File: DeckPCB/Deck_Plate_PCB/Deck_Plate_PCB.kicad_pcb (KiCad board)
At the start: 2 copper layers, 101.6 x 53.3 mm, 29 parts, among them J1 Raspberry_Pi_2_3, J2 DB37_Male_MountingHoles, J3 NASA PWR_Interface, P1 Digital, P10 CONN_01X01, P11 CONN_01X01, P12 CONN_01X01, P13 CONN_01X01, P2 Power, P3 Analog, P4 Analog, P5 PWM, P6 PWM, P7 Communication, P8 CONN_01X01, P9 CONN_01X01, Q2 2N7000, Q3 2N7000, U1 Adafruit_INA219_Breakout, U2 LM2576T-5, U3 D24V25F9, U4 SunnyBuddy_Breakout, U5 LM2576T-5, U6 SF_Logic_Level_Conv, U7 LIDAR-LITE_V4_Range, U8 ADXL377

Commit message: Updated RaspPi connections based on input from Software. Updated footprints from capacitor and inductor changes. Added inhibit header for batter, motor, and burn-wire.
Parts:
- added C1: 1000uF, Deck_Plate_PCB:1000uF_Cap, F.Cu at (307.2, 140.2)
- added C2: 1000uF, Deck_Plate_PCB:1000uF_Cap, F.Cu at (293.2, 140.2)
- added C3: 1uF, Capacitor_SMD:C_1206_3216Metric_Pad1.42x1.75mm_HandSolder, F.Cu at (283.4, 124.0)
- added C4: 1uF, Capacitor_SMD:C_1206_3216Metric_Pad1.42x1.75mm_HandSolder, F.Cu at (283.7, 126.7)
- added C5: 220uF, Deck_Plate_PCB:220uF_Cap, F.Cu at (326.8, 135.8)
- added D1: LED, LED_THT:LED_D3.0mm_Clear, F.Cu at (289.7, 125.3)
- added H1: Sunny, MountingHole:MountingHole_2.5mm, F.Cu at (229.7, 106.7)
- added H10: ADXL377, MountingHole:MountingHole_2.5mm, F.Cu at (216.1, 99.2)
- added H11: ADXL377, MountingHole:MountingHole_2.5mm, F.Cu at (216.3, 106.7)
- added H12: ADXL377, MountingHole:MountingHole_2.5mm, F.Cu at (241.8, 99.2)
- added H2: Sunny, MountingHole:MountingHole_2.5mm, F.Cu at (222.8, 113.3)
- added H3: Sunny, MountingHole:MountingHole_2.5mm, F.Cu at (229.2, 99.2)
- added H4: Sunny, MountingHole:MountingHole_2.5mm, F.Cu at (235.3, 105.7)
- added H5: INA219, MountingHole:MountingHole_2.5mm, F.Cu at (222.6, 99.2)
- added H6: INA219, MountingHole:MountingHole_2.5mm, F.Cu at (229.4, 113.3)
- added H7: INA219, MountingHole:MountingHole_2.5mm, F.Cu at (235.3, 99.2)
- added H8: INA219, MountingHole:MountingHole_2.5mm, F.Cu at (216.3, 113.3)
- added H9: ADXL377, MountingHole:MountingHole_2.5mm, F.Cu at (222.8, 106.7)
- added J4: Inhibit_Header, Connector_PinHeader_2.54mm:PinHeader_1x06_P2.54mm_Vertical, F.Cu at (66.9, 218.0)
- added L1: 100uH, Inductor_THT:L_Axial_L5.3mm_D2.2mm_P2.54mm_Vertical_Vishay_IM-1, F.Cu at (282.4, 133.0)
- added L2: 100uH, Inductor_THT:L_Axial_L5.3mm_D2.2mm_P2.54mm_Vertical_Vishay_IM-1, F.Cu at (288.5, 132.9)
- added R1: 220, Resistor_THT:R_Axial_DIN0207_L6.3mm_D2.5mm_P10.16mm_Horizontal, F.Cu at (252.1, 132.1)
- added R10: 10K, Resistor_THT:R_Axial_DIN0207_L6.3mm_D2.5mm_P10.16mm_Horizontal, F.Cu at (252.0, 124.4)
- added R11: 5K, Resistor_THT:R_Axial_DIN0207_L6.3mm_D2.5mm_P10.16mm_Horizontal, F.Cu at (252.0, 128.4)
- added R12: 5K, Resistor_THT:R_Axial_DIN0207_L6.3mm_D2.5mm_P10.16mm_Horizontal, F.Cu at (265.4, 124.4)
- added R13: 10K, Resistor_THT:R_Axial_DIN0207_L6.3mm_D2.5mm_P10.16mm_Horizontal, F.Cu at (252.0, 135.8)
- added R2: 1K, Resistor_THT:R_Axial_DIN0207_L6.3mm_D2.5mm_P10.16mm_Horizontal, F.Cu at (238.0, 140.5)
- added R3: R, Resistor_THT:R_Axial_DIN0207_L6.3mm_D2.5mm_P10.16mm_Horizontal, F.Cu at (238.0, 136.5)
- added R4: 1K, Resistor_THT:R_Axial_DIN0207_L6.3mm_D2.5mm_P10.16mm_Horizontal, F.Cu at (265.3, 136.4)
- added R5: R, Resistor_THT:R_Axial_DIN0207_L6.3mm_D2.5mm_P10.16mm_Horizontal, F.Cu at (238.0, 132.4)
- added R6: 10K, Resistor_THT:R_Axial_DIN0207_L6.3mm_D2.5mm_P10.16mm_Horizontal, F.Cu at (238.0, 128.4)
- added R7: 10K, Resistor_THT:R_Axial_DIN0207_L6.3mm_D2.5mm_P10.16mm_Horizontal, F.Cu at (265.4, 128.4)
- added R8: 5K, Resistor_THT:R_Axial_DIN0207_L6.3mm_D2.5mm_P10.16mm_Horizontal, F.Cu at (265.3, 132.4)
- added R9: 5K, Resistor_THT:R_Axial_DIN0207_L6.3mm_D2.5mm_P10.16mm_Horizontal, F.Cu at (238.0, 124.3)
- added U10: LM20, Deck_Plate_PCB:LM20, F.Cu at (86.1, 206.0)
- added U11: Big_Easy_Driver, Deck_Plate_PCB:Big_Easy_Driver, F.Cu at (56.6, 237.8)
- added U13: LM20, Deck_Plate_PCB:LM20, F.Cu at (81.2, 205.9)
- added U14: Sunny_Batt, Connector_JST:JST_PH_B2B-PH-K_1x02_P2.00mm_Vertical, F.Cu at (75.2, 203.1)
- added U9: TTL_Camera, Connector_PinHeader_2.54mm:PinHeader_1x04_P2.54mm_Vertical, F.Cu at (66.5, 202.6)
- J2: value DB37_Male_MountingHoles -> NASA_Telemetry_Interface
- moved Q2 38.2 mm to (228.0, 125.4)
- moved Q3 38.2 mm to (228.0, 131.2)
- moved U2 27.1 mm to (214.1, 125.8)
- moved D2 26.8 mm to (190.7, 125.0)
- moved D3 24.4 mm to (190.9, 134.2)
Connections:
- net /Bit_16 renamed Net-(J1-Pad22)
- J1 pad 15: /Bit_13 -> Net-(J1-Pad15)
- J1 pad 16: /Bit_14 -> Net-(J1-Pad16)
- J1 pad 18: /Bit_15 -> Net-(J1-Pad18)
- J1 pad 21: /Bit_10 -> Net-(J1-Pad21)
- J1 pad 24: /Bit_9 -> /Strobe
- J1 pad 26: /Bit_8 -> /Bit_7
- J1 pad 27: /Bit_1 -> /Bit_0
- J1 pad 28: /Bit_2 -> /Bit_1
- J1 pad 29: /Bit_6 -> /Bit_5
- J1 pad 3: /Bit_3 -> /Bit_2
- J1 pad 31: /Bit_7 -> /Bit_6
- J1 pad 37: /Strobe -> Net-(J1-Pad37)
- J1 pad 38: /Bit_11 -> Net-(J1-Pad38)
- J1 pad 40: /Bit_12 -> Net-(J1-Pad40)
- J1 pad 5: /Bit_4 -> /Bit_3
- J1 pad 7: /Bit_5 -> /Bit_4
- J2 pad 0: Net-(J2-Pad0) -> GND
- J3 pad 0: Net-(J3-Pad0) -> GND
- U6 pad 1: /2(**) -> Net-(U6-Pad1)
- U6 pad 2: /3(**) -> Net-(U6-Pad2)
- U6 pad 7: /GPIO_A -> Net-(U6-Pad7)
- U6 pad 8: /GPIO_B -> Net-(U6-Pad8)
- U6 pad 9: /??? -> /3v3_Range
- U7 pad 1: /5V_Bus_2 -> /3v3_Range

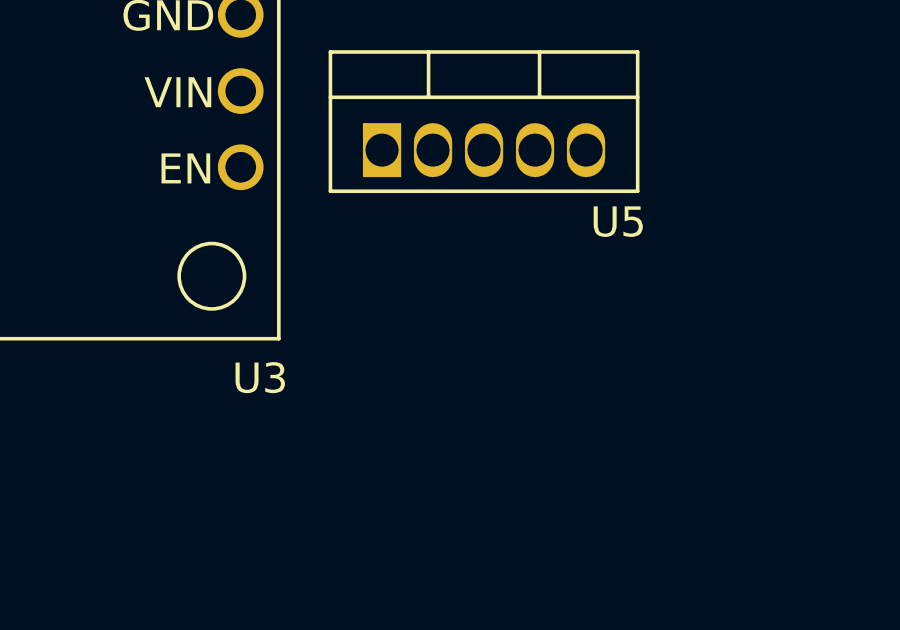
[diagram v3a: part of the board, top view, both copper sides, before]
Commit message: Assigned signals between arduino and sensors based on software input.
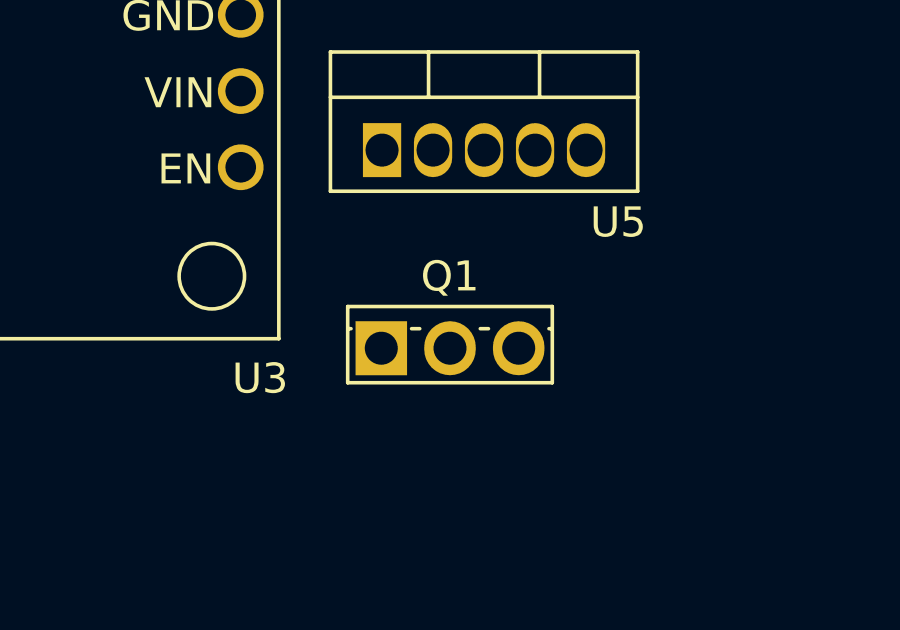
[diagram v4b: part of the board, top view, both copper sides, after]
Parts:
- added Q1: Q_NPN_BCE, Package_TO_SOT_THT:TO-251-3_Vertical, F.Cu at (164.1, 140.7)
- R3, R5: value R -> 4.7
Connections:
- net /24 renamed /Digital_24
- net /25 renamed /Digital_25
- net /26 renamed /Digital_26
- net /27 renamed /Digital_27
- net /28 renamed /Digital_28
- net /29 renamed /Digital_29
- net /30 renamed /Digital_30
- net /31 renamed /Digital_31
- net /32 renamed /Digital_32
- net /33 renamed /Digital_33
- net /34 renamed /Digital_34
- net /35 renamed /Digital_35
- net /36 renamed /Digital_36
- net /37 renamed /Digital_37
- net /38 renamed /Digital_38
- net /39 renamed /Digital_39
- net /40 renamed /Digital_40
- net /41 renamed /Digital_41
- net /42 renamed /Digital_42
- net /44 renamed /Digital_44
- net /45 renamed /Digital_45
- net /46 renamed /Digital_46
- net /47 renamed /Digital_47
- net /48 renamed /Digital_48
- net /49 renamed /Digital_49
- net /TE_Ra renamed /TE_RA
- net /TE_Rb renamed /TE_RB
- P1 pad 14: /43 -> /BurnWireSignal
- P1 pad 33: /22 -> /TE_B
- P1 pad 34: /23 -> /TE_A
- P4 pad 1: /A8 -> /Xout
- P4 pad 2: /A9 -> /Yout
- P4 pad 3: /A10 -> /Zout
- P4 pad 7: /A14 -> /PayloadTemp
- P4 pad 8: /A15 -> /SolarArrayTemp
- P7 pad 5: /18(Tx1) -> /TTL_TX
- P7 pad 6: /19(Rx1) -> /TTL_RX
- R3 pad 1: Net-(Q1-Pad1) -> Net-(Q1-Pad3)
- R3 pad 2: /BurnWireSignal -> GND
- R5 pad 1: /5V_Bus_1 -> Net-(Q1-Pad3)
- R5 pad 2: Net-(Q1-Pad2) -> GND
- U1 pad 3: /SCL -> /21(SCL)
- U1 pad 4: /SDA -> /20(SDA)
- U2 pad 1: /NASA_28V -> /28V_GSE_2
- U5 pad 1: /NASA_28V -> /28V_GSE_2
- U8 pad 5: /A0 -> /Zout
- U8 pad 6: /A1 -> /Yout
- U8 pad 7: /A2 -> /Xout

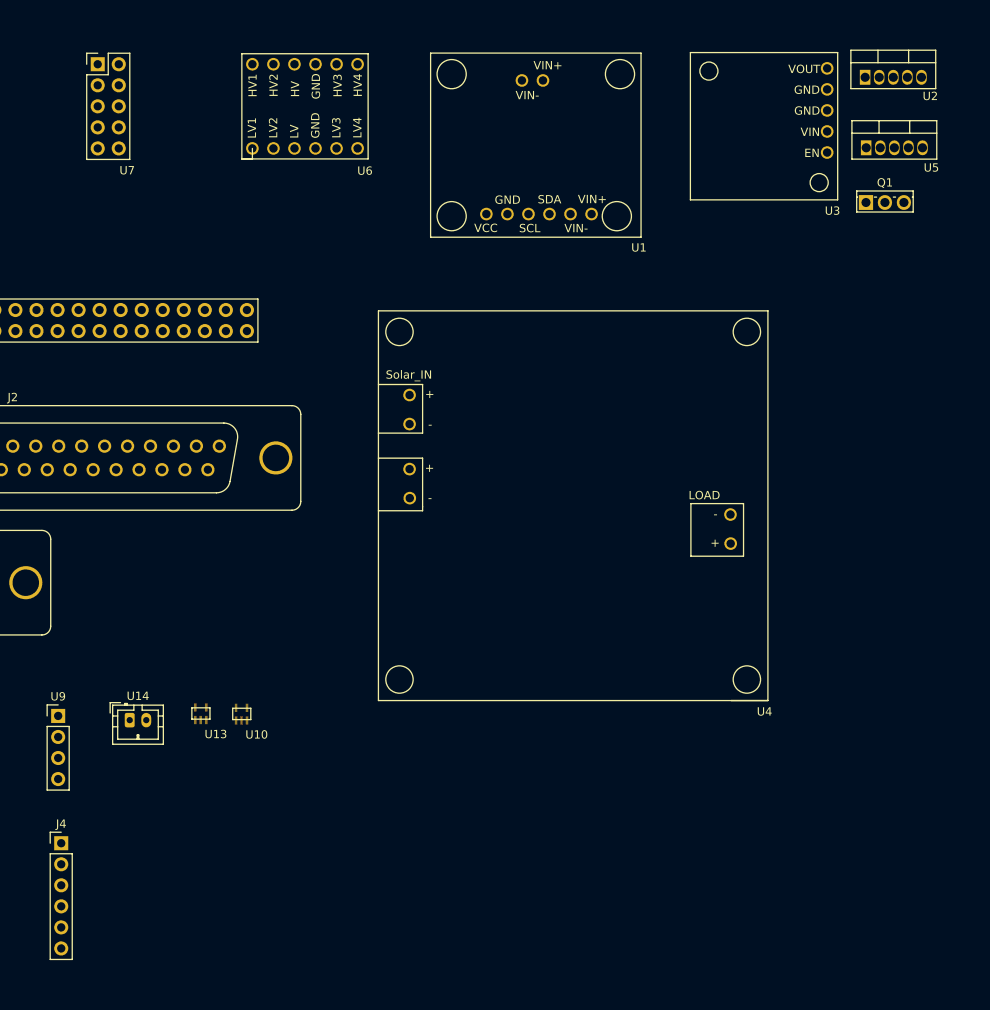
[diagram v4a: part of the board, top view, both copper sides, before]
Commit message: Updated connections to Logic Level Shifter and LiDAR sensor. Updated inhibit connection scheme.
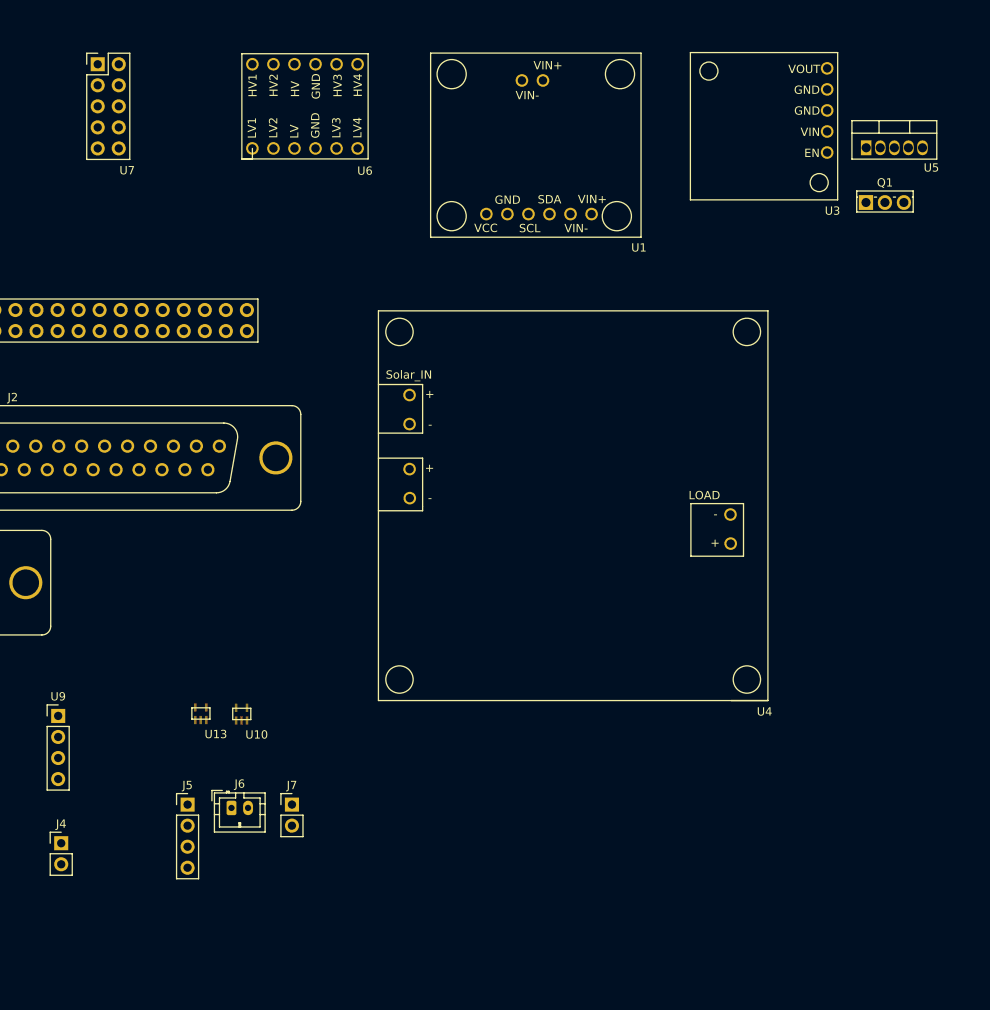
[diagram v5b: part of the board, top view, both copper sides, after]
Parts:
- removed U14: Sunny_Batt, Connector_JST:JST_PH_B2B-PH-K_1x02_P2.00mm_Vertical
- removed the U2 at (164.0, 125.6)
- added J5: SunnyBuddy_Inhibit, Connector_PinHeader_2.54mm:PinHeader_1x04_P2.54mm_Vertical, F.Cu at (82.2, 213.3)
- added J6: Batt_JST_Conn, Connector_JST:JST_PH_B2B-PH-K_1x02_P2.00mm_Vertical, F.Cu at (87.5, 213.7)
- added J7: BurWire_Inhibit, Connector_PinHeader_2.54mm:PinHeader_1x02_P2.54mm_Vertical, F.Cu at (94.8, 213.3)
- J4: value Inhibit_Header -> Motor_Inhibit; footprint Connector_PinHeader_2.54mm:PinHeader_1x06_P2.54mm_Vertical -> Connector_PinHeader_2.54mm:PinHeader_1x02_P2.54mm_Vertical
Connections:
- net /Analog_10 renamed Net-(J2-Pad10)
- net /Analog_4 renamed /NASA_Analog_4
- net /Analog_5 renamed Net-(J2-Pad5)
- net /Analog_6 renamed Net-(J2-Pad6)
- net /Analog_7 renamed Net-(J2-Pad7)
- net /Analog_8 renamed Net-(J2-Pad8)
- net /Analog_9 renamed Net-(J2-Pad9)
- net /Bit_10 renamed Net-(J2-Pad23)
- net /Bit_11 renamed Net-(J2-Pad24)
- net /Bit_12 renamed Net-(J2-Pad25)
- net /Bit_13 renamed Net-(J2-Pad26)
- net /Bit_14 renamed Net-(J2-Pad27)
- net /Bit_15 renamed Net-(J2-Pad28)
- net /Bit_16_LSB renamed Net-(J2-Pad29)
- net /Bit_1_MSB renamed Net-(J2-Pad11)
- net /Bit_8 renamed Net-(J2-Pad21)
- net /Bit_9 renamed Net-(J2-Pad22)
- net /GPIO_A renamed Net-(U7-Pad5)
- net /GPIO_B renamed Net-(U7-Pad6)
- net /LED+ renamed Net-(R1-Pad1)
- J2 pad 1: /Analog_1 -> /NASA_Analog_1
- J2 pad 2: /Analog_2 -> /NASA_Analog_2
- J2 pad 3: /Analog_3 -> /NASA_Analog_3
- J4 pad 1: /Sunny_Batt -> /9V_Bus
- J4 pad 2: GND -> /9V_Bus
- P6 pad 4: /4(**) -> /NASA_Analog_3
- P6 pad 5: /3(**) -> /NASA_Analog_2
- P6 pad 6: /2(**) -> /NASA_Analog_1
- U6 pad 9: /3v3_Range -> +3V3
- U7 pad 1: /3v3_Range -> /5V_Bus_1

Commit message: Initial PCB component placement finished. All mounting holes in place. NOT REPRESENTED: SunnyBuddy, INA219, Electrical inhibits, Motor circuitry, sensor end-panel circuitry. Will create daughter board for these components along with placement for the RaspPi next.
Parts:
- removed H11, H12: ADXL377, MountingHole:MountingHole_2.5mm
- removed H5, H6, H7, H8: INA219, MountingHole:MountingHole_2.5mm
- added H13: Enclos, MountingHole:MountingHole_3.5mm, F.Cu at (45.7, 20.4)
- added H14: Enclos, MountingHole:MountingHole_3.5mm, F.Cu at (45.8, 110.5)
- added H15: Enclos, MountingHole:MountingHole_3.5mm, F.Cu at (155.8, 20.4)
- added H16: Enclos, MountingHole:MountingHole_3.5mm, F.Cu at (155.8, 110.5)
- H1, H2: value Sunny -> 9V_mount; footprint MountingHole:MountingHole_2.5mm -> MountingHole:MountingHole_2.2mm_M2
- H10, H9: value ADXL377 -> Accel_mount
- H3, H4: value Sunny -> Accel_mount
- J2: footprint Connector_Dsub:DSUB-37_Male_Vertical_P2.77x2.84mm_MountingHoles -> Deck_Plate_PCB:NASA_Telem_37-pin_DSub
- J3: footprint Connector_Dsub:DSUB-15_Male_Vertical_P2.77x2.84mm_MountingHoles -> Deck_Plate_PCB:NASA_PWR_15-pin_DSub
- U7: value LIDAR-LITE_V4_Range -> Lidar_RangeFinder; footprint Connector_PinHeader_2.54mm:PinHeader_2x05_P2.54mm_Vertical -> Connector_PinHeader_2.54mm:PinHeader_1x04_P2.54mm_Vertical
- moved C4 326.9 mm to (-41.4, 160.8)
- moved C3 326.2 mm to (-41.7, 149.9)
- moved R4 322.7 mm to (-56.5, 160.7)
- moved D1 319.6 mm to (-20.4, 48.4)
- moved R3 286.6 mm to (-48.5, 129.3)
- moved R2 284.4 mm to (-46.3, 149.8), turned to 180 degrees
- moved R5 277.5 mm to (-39.4, 123.7)
- moved R1 271.8 mm to (-10.5, 61.9), turned to 180 degrees
- moved U4 222.9 mm to (-48.8, -7.44)
- moved R7 216.7 mm to (51.9, 90.6), turned to 180 degrees
- moved Q1 215.9 mm to (-51.0, 121.6)
- moved C5 212.4 mm to (115.4, 116.0)
- moved R8 196.7 mm to (73.8, 87.2), turned to 90 degrees
- moved R6 190.7 mm to (51.9, 86.8), turned to 180 degrees
- moved J5 190.4 mm to (-12.3, 48.0)
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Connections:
- net /28V_GSE_1 renamed Net-(J3-Pad1)
- net /TE-1 renamed Net-(J3-Pad4)
- net /TE-2 renamed Net-(J3-Pad10)
- net /TE-3 renamed Net-(J3-Pad11)
- R11 pad 1: /TE_RB -> /TE-RB
- R8 pad 1: /TE_RA -> /TE-RA
- U1 pad 5: /Solar_IN- -> /Solar_IN+
- U1 pad 6: /Solar_IN+ -> /SolarCell+
- U4 pad 1: /Solar_IN+ -> /Solar_IN-
- U4 pad 2: /Solar_IN- -> /Solar_IN+
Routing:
- net GND: track 0.00 -> 24.7 mm, vias 0 -> 3
- net (no net): vias 4 -> 0
- added copper zone on B.Cu, net GND
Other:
- board size 101.6 x 53.3 mm -> 124.7 x 104.6 mm

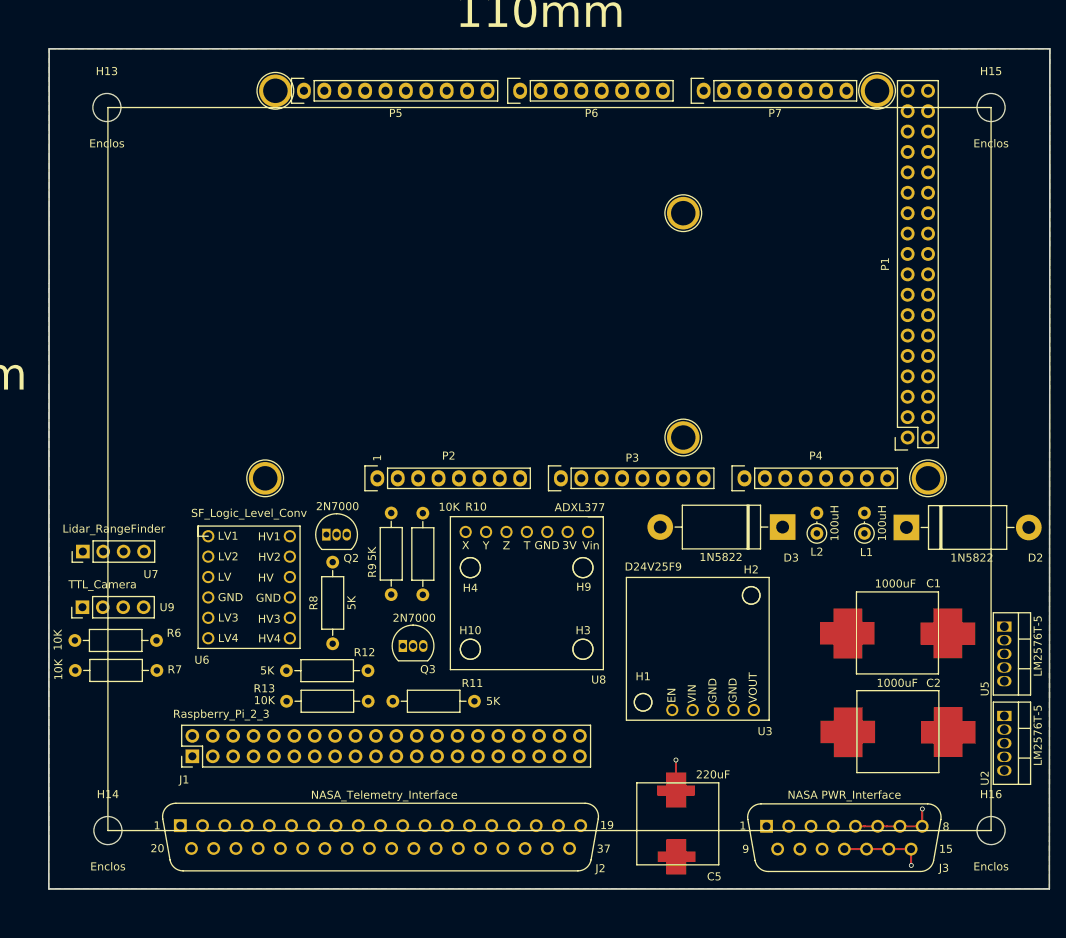
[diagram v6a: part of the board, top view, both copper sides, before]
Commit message: Created new daughter board for SunnyBuddy and RaspPi. Initial component layout complete.
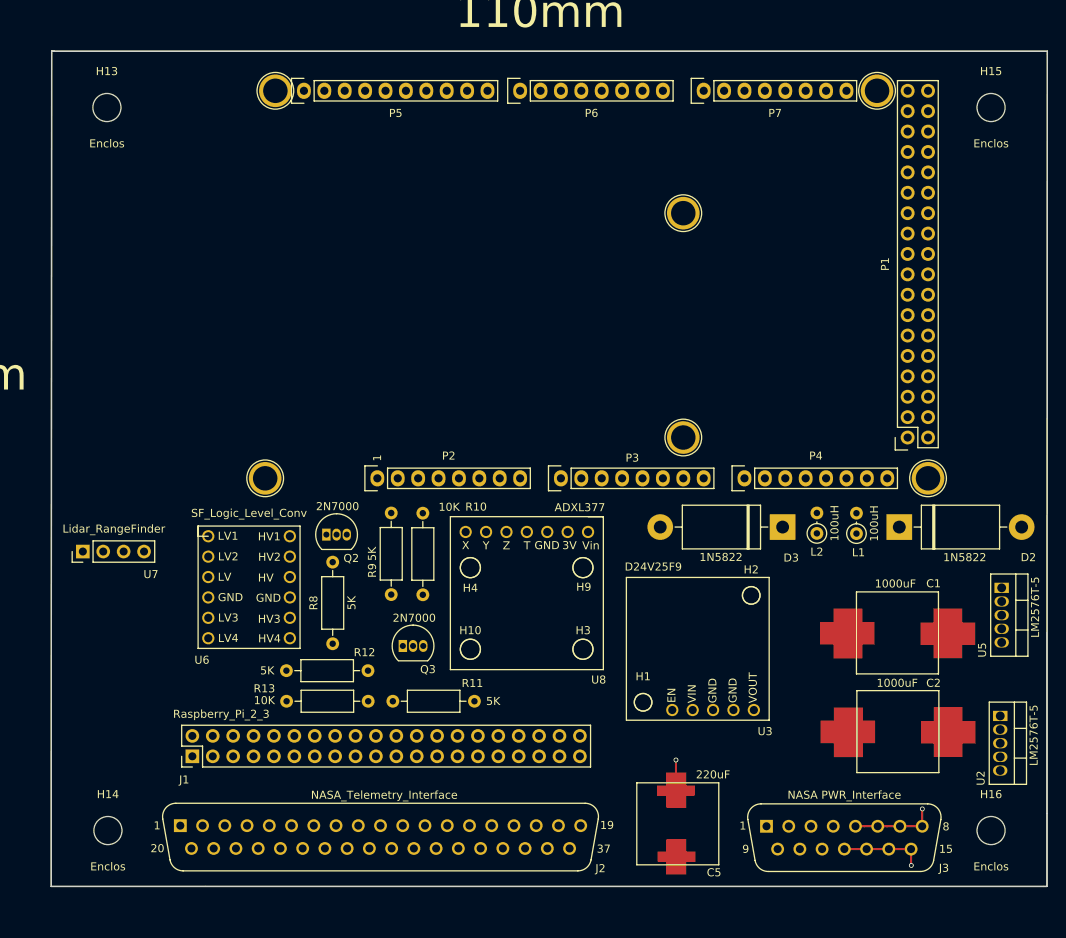
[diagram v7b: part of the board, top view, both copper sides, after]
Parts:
- removed R6, R7: 10K, Resistor_THT:R_Axial_DIN0207_L6.3mm_D2.5mm_P10.16mm_Horizontal
- removed U9: TTL_Camera, Connector_PinHeader_2.54mm:PinHeader_1x04_P2.54mm_Vertical
- moved U5 4.84 mm to (157.1, 80.3)
- moved L1 0.99 mm to (139.1, 73.5)
- moved D2 0.89 mm to (144.4, 72.7)
- moved U2 0.51 mm to (157.0, 96.2)
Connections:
- J1 pad 10: Net-(J1-Pad10) -> /TTL_RX
- P1 pad 31: /Digital_24 -> /Dir
- P1 pad 32: /Digital_25 -> /Step
- P6 pad 3: /5(**) -> /NASA_Analog_4
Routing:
- removed copper zone on B.Cu, net GND
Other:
- board size 124.7 x 104.6 mm -> 124.1 x 104 mm
